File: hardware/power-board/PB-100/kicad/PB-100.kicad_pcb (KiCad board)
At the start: 4 copper layers, 150 x 90 mm, 36 parts, among them Q1 IAUT300N08S5N012ATMA2, Q101 IAUT300N08S5N012ATMA2, Q102 IAUT300N08S5N012ATMA2, Q103 IAUT300N08S5N012ATMA2, Q104 IAUT300N08S5N012ATMA2, Q105 IAUT300N08S5N012ATMA2, Q106 IAUT300N08S5N012ATMA2, Q107 IAUT300N08S5N012ATMA2, Q108 IAUT300N08S5N012ATMA2, Q109 IAUT300N08S5N012ATMA2, Q110 IAUT300N08S5N012ATMA2, Q2 IAUTN15S6N025ATMA1, U1 LM74930QRGERQ1

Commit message: feat: add dual protected fog switch inputs
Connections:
- net EXT_DIG2 renamed FOG_B_SW_IN
- net FOG_SW_IN renamed FOG_A_SW_IN
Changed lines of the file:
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@@
 	(net 15 "EXT_ADC1")
 	(net 16 "EXT_ADC2")
-	(net 17 "EXT_DIG2")
-	(net 18 "FOG_SW_IN")
+	(net 17 "FOG_A_SW_IN")
+	(net 18 "FOG_B_SW_IN")
 	(net 19 "GND")
 	(net 20 "IIN_SENSE")
@@
 			(layers "F.Cu" "F.Paste" "F.Mask")
 			(roundrect_rratio 0.200)
-			(net 18 "FOG_SW_IN")
-			(pinfunction "FOG_SW_IN")
+			(net 17 "FOG_A_SW_IN")
+			(pinfunction "FOG_A_SW_IN")
 			(pintype "passive")
 		)
@@
 			(layers "F.Cu" "F.Paste" "F.Mask")
 			(roundrect_rratio 0.200)
-			(net 17 "EXT_DIG2")
-			(pinfunction "EXT_DIG2")
-			(pintype "passive")
-		)
+			(net 18 "FOG_B_SW_IN")
+			(pinfunction "FOG_B_SW_IN")
+			(pintype "passive")
+		)

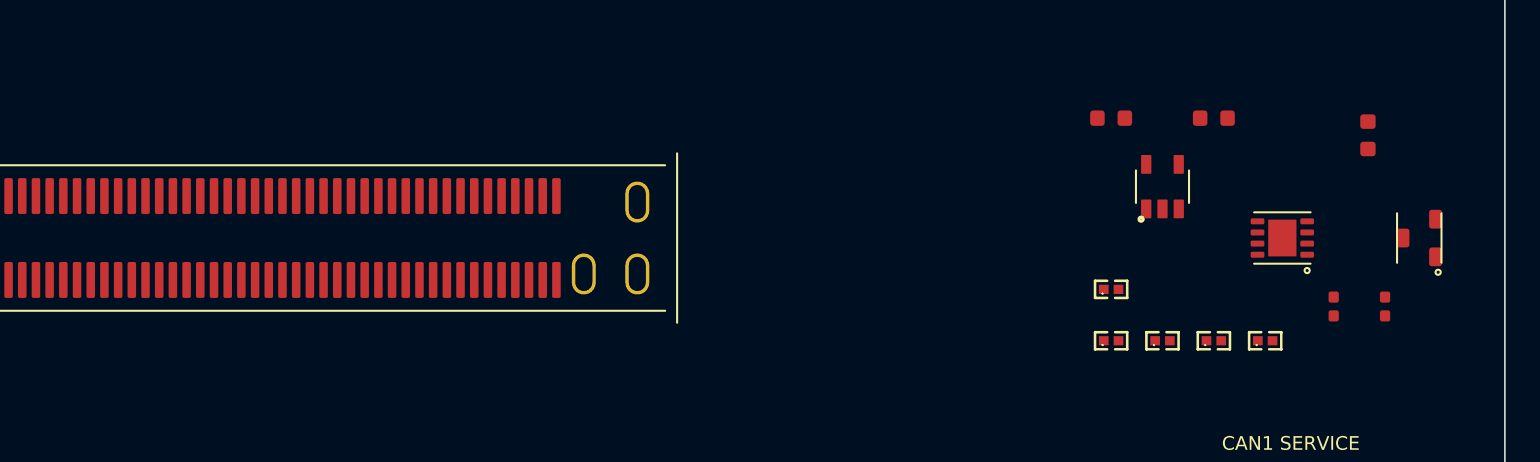
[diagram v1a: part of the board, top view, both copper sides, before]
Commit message: feat(hardware): add EVT board routing milestones
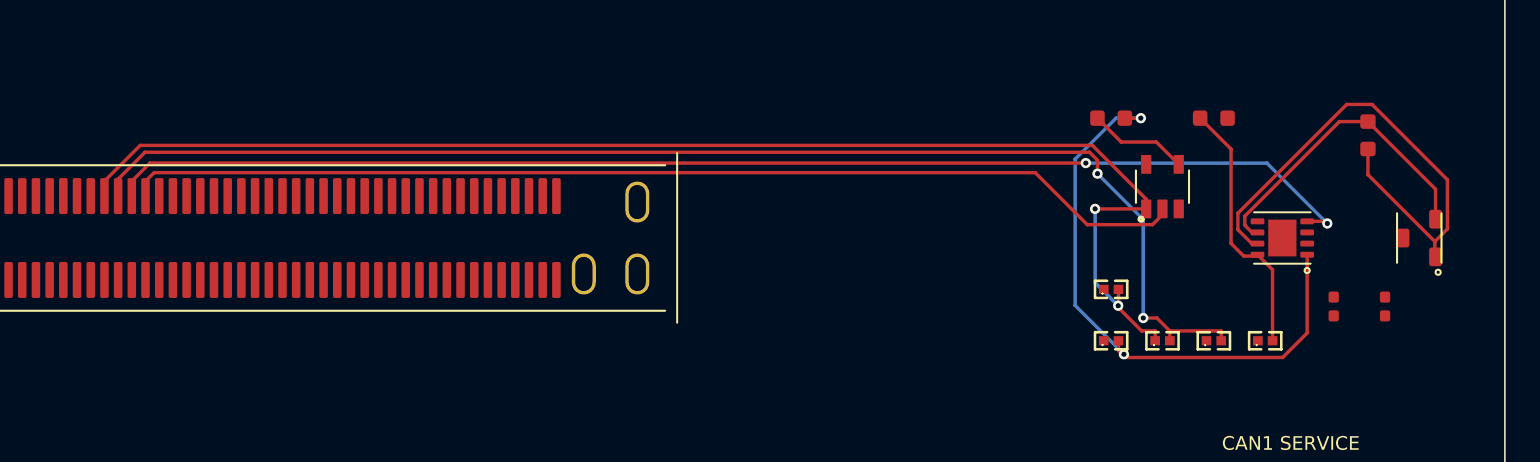
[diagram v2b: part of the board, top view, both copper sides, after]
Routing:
- net CAN1_TX_DISABLE_CMD: track 0.00 -> 78.0 mm, vias 0 -> 2
- net CAN1_TX_DISABLED_STATUS: track 0.00 -> 75.4 mm, vias 0 -> 2
- net CAN1_RX_ROUTE: track 0.00 -> 73.8 mm, vias 0 -> 2
- net CAN1_TX_ROUTE: track 0.00 -> 62.3 mm
- net CAN1_TXD_SAFE: track 0.00 -> 35.7 mm, vias 0 -> 2
- net CAN1_HARNESS_H: track 0.00 -> 31.0 mm
- net CAN1_HARNESS_L: track 0.00 -> 18.3 mm
- net CAN1_PHY_SILENT: track 0.00 -> 15.3 mm
- net CAN1_TX_GATE_OUT: track 0.00 -> 5.87 mm

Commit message: hardware: correct fog entry and EVT layout gates
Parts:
- added D_FOG1: ESD2CANFD24DBZRQ1, PB100:SOT-23-3_DBZ_TI, F.Cu at (10.0, 25.5)
- added F_FOG_12V: nanoASMDC010F 0.10A 60V DNP, PB100:PPTC_1206_3216Metric, F.Cu at (17.0, 31.0)
- added JFOG1: SEALED_DTM_3WAY_PIGTAIL_ENTRY, PB100:FOG_PIGTAIL_1x03_P3.50mm, F.Cu at (4.00, 20.0)
- added R_FOG_12V: 0R FOG 12V common DNP, PB100:R0603_DNP_LINK_1608Metric, F.Cu at (13.0, 31.0)
- added R_FOG_GND: 0R FOG dry-contact common DEFAULT, PB100:R0603_DNP_LINK_1608Metric, F.Cu at (9.00, 31.0)
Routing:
- net FOG_A_SW_IN: track 0.00 -> 82.3 mm, vias 0 -> 2
- net FOG_B_SW_IN: track 0.00 -> 81.7 mm, vias 0 -> 2
- net SW_COMMON: track 0.00 -> 25.8 mm
- net GND: track 0.00 -> 7.23 mm, vias 0 -> 2
- net CAN1_TX_DISABLE_CMD: track 78.0 -> 84.1 mm
- net CAN1_TX_DISABLED_STATUS: track 75.4 -> 80.5 mm
- net CAN1_TX_ROUTE: track 62.3 -> 67.4 mm
- net CAN1_RX_ROUTE: track 73.8 -> 78.5 mm
- net SW_12V_FUSED: track 0.00 -> 4.31 mm

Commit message: Advance PB-100 EVT routing baseline
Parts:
- added C1101: 680nF 16V X7R TMR, PB100:C0603, F.Cu at (60.7, 27.9)
- added C1102: 470nF 25V X7R BST, PB100:C0603, F.Cu at (63.9, 27.9)
- added C1103: 1nF 50V C0G ISCP, PB100:C0603, F.Cu at (67.1, 27.9)
- added C1104: 100nF 100V X7R VS, PB100:C0805, F.Cu at (48.1, 28.1)
- added C1105: 10nF 50V X7R IMON, PB100:C0603, F.Cu at (70.3, 27.9)
- added C1106: 1nF 25V DNP GATE-SLEW, PB100:C0603, F.Cu at (43.5, 30.6)
- added C1107: 1nF 100V C0G DNP SNUBBER, PB100:C0603, F.Cu at (46.6, 30.6)
- added C1201: 680nF 16V X7R TMR, PB100:C0603, F.Cu at (84.8, 27.9)
- added C1202: 470nF 25V X7R BST, PB100:C0603, F.Cu at (88.0, 27.9)
- added C1203: 1nF 50V C0G ISCP, PB100:C0603, F.Cu at (100.7, 27.9)
- added C1204: 100nF 100V X7R VS, PB100:C0805, F.Cu at (81.3, 28.1)
- added C1205: 10nF 50V X7R IMON, PB100:C0603, F.Cu at (103.9, 27.9)
- added C1206: 1nF 25V DNP GATE-SLEW, PB100:C0603, F.Cu at (78.5, 30.6)
- added C1207: 1nF 100V C0G DNP SNUBBER, PB100:C0603, F.Cu at (81.7, 30.6)
- added C1301: 680nF 16V X7R TMR, PB100:C0603, F.Cu at (19.8, 6.25)
- added C1302: 470nF 25V X7R BST, PB100:C0603, F.Cu at (22.9, 6.25)
- added C1303: 1nF 50V C0G ISCP, PB100:C0603, F.Cu at (16.1, 8.95)
- added C1304: 100nF 100V X7R VS, PB100:C0805, F.Cu at (16.4, 6.45)
- added C1305: 10nF 50V X7R IMON, PB100:C0603, F.Cu at (19.4, 8.95)
- added C1306: 1nF 25V DNP GATE-SLEW, PB100:C0603, F.Cu at (22.6, 8.95)
- added C1307: 1nF 100V C0G DNP SNUBBER, PB100:C0603, F.Cu at (13.4, 10.8)
- added C1401: 680nF 16V X7R TMR, PB100:C0603, F.Cu at (32.0, 6.25)
- added C1402: 470nF 25V X7R BST, PB100:C0603, F.Cu at (35.2, 6.25)
- added C1403: 1nF 50V C0G ISCP, PB100:C0603, F.Cu at (38.5, 6.25)
- added C1404: 100nF 100V X7R VS, PB100:C0805, F.Cu at (28.6, 6.45)
- added C1405: 10nF 50V X7R IMON, PB100:C0603, F.Cu at (32.0, 8.45)
- added C1406: 1nF 25V DNP GATE-SLEW, PB100:C0603, F.Cu at (35.2, 8.45)
- added C1407: 1nF 100V C0G DNP SNUBBER, PB100:C0603, F.Cu at (38.5, 8.45)
- added C1501: 680nF 16V X7R TMR, PB100:C0603, F.Cu at (49.9, 35.0)
- added C1502: 470nF 25V X7R BST, PB100:C0603, B.Cu at (49.0, 10.2)
- added C1503: 1nF 50V C0G ISCP, PB100:C0603, B.Cu at (52.2, 10.2)
- added C1504: 100nF 100V X7R VS, PB100:C0805, B.Cu at (45.6, 10.4)
- added C1505: 10nF 50V X7R IMON, PB100:C0603, F.Cu at (53.0, 35.0)
- added C1506: 1nF 25V DNP GATE-SLEW, PB100:C0603, F.Cu at (45.5, 36.8)
- added C1507: 1nF 100V C0G DNP SNUBBER, PB100:C0603, F.Cu at (48.6, 36.8)
- added C1601: 680nF 16V X7R TMR, PB100:C0603, F.Cu at (64.2, 6.25)
- added C1602: 470nF 25V X7R BST, PB100:C0603, B.Cu at (65.0, 2.75)
- added C1603: 1nF 50V C0G ISCP, PB100:C0603, B.Cu at (68.2, 2.75)
- added C1604: 100nF 100V X7R VS, PB100:C0805, B.Cu at (61.6, 2.95)
- added C1605: 10nF 50V X7R IMON, PB100:C0603, F.Cu at (67.3, 6.25)
- added C1606: 1nF 25V DNP GATE-SLEW, PB100:C0603, B.Cu at (71.5, 2.75)
- added C1607: 1nF 100V C0G DNP SNUBBER, PB100:C0603, B.Cu at (65.0, 4.95)
- added C1701: 680nF 16V X7R TMR, PB100:C0603, F.Cu at (77.5, 6.25)
- added C1702: 470nF 25V X7R BST, PB100:C0603, B.Cu at (83.8, 2.75)
- added C1703: 1nF 50V C0G ISCP, PB100:C0603, B.Cu at (87.0, 2.75)
- added C1704: 100nF 100V X7R VS, PB100:C0805, B.Cu at (80.3, 2.95)
- added C1705: 10nF 50V X7R IMON, PB100:C0603, F.Cu at (80.7, 6.25)
- added C1706: 1nF 25V DNP GATE-SLEW, PB100:C0603, B.Cu at (80.2, 5.45)
- added C1707: 1nF 100V C0G DNP SNUBBER, PB100:C0603, B.Cu at (83.3, 5.45)
- added C1801: 680nF 16V X7R TMR, PB100:C0603, F.Cu at (93.5, 35.0)
- added C1802: 470nF 25V X7R BST, PB100:C0603, B.Cu at (97.0, 10.2)
- added C1803: 1nF 50V C0G ISCP, PB100:C0603, B.Cu at (100.2, 10.2)
- added C1804: 100nF 100V X7R VS, PB100:C0805, B.Cu at (93.7, 10.4)
- added C1805: 10nF 50V X7R IMON, PB100:C0603, F.Cu at (93.5, 36.8)
- added C1806: 1nF 25V DNP GATE-SLEW, PB100:C0603, B.Cu at (103.5, 10.2)
- added C1807: 1nF 100V C0G DNP SNUBBER, PB100:C0603, F.Cu at (103.8, 36.8)
- added C1901: 680nF 16V X7R TMR, PB100:C0603, F.Cu at (113.0, 33.0)
- added C1902: 470nF 25V X7R BST, PB100:C0603, F.Cu at (109.5, 35.2)
- added C1903: 1nF 50V C0G ISCP, PB100:C0603, F.Cu at (112.7, 35.2)
- added C1904: 100nF 100V X7R VS, PB100:C0805, F.Cu at (109.7, 33.2)
- added C1905: 10nF 50V X7R IMON, PB100:C0603, F.Cu at (109.5, 37.0)
- added C1906: 1nF 25V DNP GATE-SLEW, PB100:C0603, F.Cu at (112.7, 37.0)
- added C1907: 1nF 100V C0G DNP SNUBBER, PB100:C0603, F.Cu at (115.8, 37.0)
- added C20: 100nF 50V X7R DIFF, PB100:C0603, B.Cu at (26.3, 25.1)
- added C2001: 680nF 16V X7R TMR, PB100:C0603, F.Cu at (132.8, 6.25)
- added C2002: 470nF 25V X7R BST, PB100:C0603, F.Cu at (135.9, 6.25)
- added C2003: 1nF 50V C0G ISCP, PB100:C0603, F.Cu at (129.2, 8.95)
- added C2004: 100nF 100V X7R VS, PB100:C0805, F.Cu at (129.3, 6.45)
- added C2005: 10nF 50V X7R IMON, PB100:C0603, F.Cu at (132.3, 8.95)
- added C2006: 1nF 25V DNP GATE-SLEW, PB100:C0603, F.Cu at (135.6, 8.95)
- added C2007: 1nF 100V C0G DNP SNUBBER, PB100:C0603, F.Cu at (129.4, 10.8)
- added C21: 1nF 100V C0G, PB100:C0603, B.Cu at (29.5, 25.1)
- added C22: 100nF 16V X7R, PB100:C0603, B.Cu at (32.7, 25.1)
- added C23: 1nF PB I2C INT FILTER DNP, PB100:C0603, B.Cu at (7.55, 27.9)
- added C24: 10nF 50V X7R, PB100:C0603, B.Cu at (10.8, 27.9)
- added C30: 2.2uF 100V X7R, PB100:C1210, F.Cu at (114.0, 8.00)
- added C31: 100nF 100V X7R, PB100:C0805, F.Cu at (118.0, 8.00)
- added C32: 10uF 100V BULK CANDIDATE, PB100:C1210, F.Cu at (114.0, 15.5)
- added C33: 2.2nF 50V X7R, PB100:C0603, F.Cu at (119.0, 14.0)
- added C34: 22uF 10V X7R, PB100:C1210, F.Cu at (137.0, 22.0)
- added C35: 22uF 10V X7R, PB100:C1210, F.Cu at (137.0, 28.0)
- added C36: 100nF 16V X7R, PB100:C0603, F.Cu at (137.0, 34.0)
- added C37: 10nF PGOOD FILTER DNP, PB100:C0603, B.Cu at (121.5, 43.5)
- added C38: 3.3nF 100V C0G TYPE3 CA, PB100:C0603, F.Cu at (144.0, 15.0)
- added C39: 180pF 50V C0G TYPE3 CB, PB100:C0603, F.Cu at (144.0, 23.0)
- added C40: 1nF 100V C0G DNP, PB100:C0603, F.Cu at (132.0, 34.0)
- added C61: 10nF 50V X7R, PB100:C0603, B.Cu at (124.7, 43.5)
- added C64: 10nF 50V X7R, PB100:C0603, B.Cu at (127.8, 43.5)
- added C67: 10nF 50V X7R, PB100:C0603, B.Cu at (131.1, 43.5)
- added CCAP1: 100nF 25V X7R, PB100:C0603, B.Cu at (13.9, 27.9)
- added CSN1: 1nF 100V C0G DNP, PB100:C0603, B.Cu at (17.1, 27.9)
- added CSN2: 1nF 200V C0G DNP, PB100:C0603, B.Cu at (20.4, 27.9)
- added CVS1: CGA6N3X7R2A225M230AE 2.2uF 100V X7R; Ceff>=1uF@56V, PB100:C1210, B.Cu at (8.57, 22.6)
- added DCL101: STPS40170CGY-TR 2x20A 170V COMMON-CATHODE, PB100:D2PAK_3_CommonCathode, F.Cu at (68.0, 16.0)
- added DCL102: STPS40170CGY-TR 2x20A 170V COMMON-CATHODE, PB100:D2PAK_3_CommonCathode, F.Cu at (82.0, 16.0)
- added DCL103: STPS40170CGY-TR 2x20A 170V COMMON-CATHODE, PB100:D2PAK_3_CommonCathode, B.Cu at (16.0, 75.0)
- added DCL104: STPS40170CGY-TR 2x20A 170V COMMON-CATHODE, PB100:D2PAK_3_CommonCathode, B.Cu at (30.0, 75.0)
- added DCL105: STPS40170CGY-TR 2x20A 170V COMMON-CATHODE, PB100:D2PAK_3_CommonCathode, B.Cu at (51.0, 75.0)
- added DCL106: STPS40170CGY-TR 2x20A 170V COMMON-CATHODE, PB100:D2PAK_3_CommonCathode, B.Cu at (67.0, 75.0)
- added DCL107: STPS40170CGY-TR 2x20A 170V COMMON-CATHODE, PB100:D2PAK_3_CommonCathode, B.Cu at (83.0, 75.0)
- added DCL108: STPS40170CGY-TR 2x20A 170V COMMON-CATHODE, PB100:D2PAK_3_CommonCathode, B.Cu at (99.0, 75.0)
- added DCL109: STPS40170CGY-TR 2x20A 170V COMMON-CATHODE, PB100:D2PAK_3_CommonCathode, B.Cu at (120.0, 75.0)
- added DCL110: STPS40170CGY-TR 2x20A 170V COMMON-CATHODE, PB100:D2PAK_3_CommonCathode, B.Cu at (134.0, 75.0)
- added DZVS1: 56V AUTOMOTIVE ZENER, PB100:SOD-123F, B.Cu at (14.0, 22.4)
- added JIN1: 40A PCB PIGTAIL TO NEAR-BATTERY 50A FUSE, PB100:POWER_PIGTAIL_2xTH_40A, F.Cu at (6.50, 45.0)
- added JISO1: EVT INPUT-STAGE ISOLATION LINK — FITTED FOR NORMAL EVT, PB100:EVT_INPUT_ISOLATION_LINK_M4, F.Cu at (34.0, 44.0)
- added L1: 47uH SHIELDED AEC-Q200; Isat>=2.2A Irms>=1.2A, PB100:Inductor_12x12mm, F.Cu at (126.0, 25.0)
- added QT101: MMBT3904-Q REMOTE TEMP DIODE, PB100:SOT-23-3_DBZ_TI, F.Cu at (46.3, 22.6)
- added QT102: MMBT3904-Q REMOTE TEMP DIODE, PB100:SOT-23-3_DBZ_TI, F.Cu at (103.0, 22.6)
- added QT103: MMBT3904-Q REMOTE TEMP DIODE, PB100:SOT-23-3_DBZ_TI, F.Cu at (14.5, 3.60)
- added QT104: MMBT3904-Q REMOTE TEMP DIODE, PB100:SOT-23-3_DBZ_TI, F.Cu at (29.5, 3.60)
- added QT105: MMBT3904-Q REMOTE TEMP DIODE, PB100:SOT-23-3_DBZ_TI, F.Cu at (46.5, 11.1)
- added QT106: MMBT3904-Q REMOTE TEMP DIODE, PB100:SOT-23-3_DBZ_TI, F.Cu at (62.5, 3.60)
- added QT107: MMBT3904-Q REMOTE TEMP DIODE, PB100:SOT-23-3_DBZ_TI, F.Cu at (78.5, 3.60)
- added QT108: MMBT3904-Q REMOTE TEMP DIODE, PB100:SOT-23-3_DBZ_TI, F.Cu at (103.0, 11.1)
- added QT109: MMBT3904-Q REMOTE TEMP DIODE, PB100:SOT-23-3_DBZ_TI, F.Cu at (110.5, 30.4)
- added QT110: MMBT3904-Q REMOTE TEMP DIODE, PB100:SOT-23-3_DBZ_TI, F.Cu at (127.5, 3.60)
- added R1101: 470k 1%, PB100:R0603, F.Cu at (64.2, 30.6)
- added R1102: 103k 1%, PB100:R0603, F.Cu at (67.3, 30.6)
- added R1103: 12.4k 1%, PB100:R0603, F.Cu at (70.5, 30.6)
- added R1104: 100R 1% RSET, PB100:R0603, F.Cu at (43.5, 32.5)
- added R1105: 49.9k 1% RIWRN, PB100:R0603, F.Cu at (46.6, 32.5)
- added R1106: 3.40k 1% RISCP, PB100:R0603, F.Cu at (64.2, 32.5)
- added R1107: 12.1k 1% RIMON, PB100:R0603, F.Cu at (67.3, 32.5)
- added R1108: 1k 1% IMON ADC SERIES, PB100:R0603, F.Cu at (70.5, 32.5)
- added R1109: 100k CTL DEFAULT-OFF, PB100:R0603, F.Cu at (43.5, 34.2)
- added R1110: 3.3R 1% REPLACEABLE PU, PB100:R0603, F.Cu at (46.6, 34.2)
- added R1111: 0R REPLACEABLE PD, PB100:R0603, F.Cu at (64.2, 34.2)
- added R1112: 10k FLT PULL-UP, PB100:R0603, F.Cu at (67.3, 34.2)
- added R1113: 100R DNP DRAIN-SOURCE SNUBBER, PB100:R0603, F.Cu at (70.5, 34.2)
- added R1201: 470k 1%, PB100:R0603, F.Cu at (84.8, 30.6)
- added R1202: 103k 1%, PB100:R0603, F.Cu at (88.0, 30.6)
- added R1203: 12.4k 1%, PB100:R0603, F.Cu at (104.2, 30.6)
- added R1204: 100R 1% RSET, PB100:R0603, F.Cu at (78.5, 32.5)
- added R1205: 67.3k 1% RIWRN, PB100:R0603, F.Cu at (81.7, 32.5)
- added R1206: 2.61k 1% RISCP, PB100:R0603, F.Cu at (84.8, 32.5)
- added R1207: 12.1k 1% RIMON, PB100:R0603, F.Cu at (88.0, 32.5)
- added R1208: 1k 1% IMON ADC SERIES, PB100:R0603, F.Cu at (104.2, 32.5)
- added R1209: 100k CTL DEFAULT-OFF, PB100:R0603, F.Cu at (78.5, 34.2)
- added R1210: 3.3R 1% REPLACEABLE PU, PB100:R0603, F.Cu at (81.7, 34.2)
- added R1211: 0R REPLACEABLE PD, PB100:R0603, F.Cu at (84.8, 34.2)
- added R1212: 10k FLT PULL-UP, PB100:R0603, F.Cu at (88.0, 34.2)
- added R1213: 100R DNP DRAIN-SOURCE SNUBBER, PB100:R0603, F.Cu at (104.2, 34.2)
- added R1301: 470k 1%, PB100:R0603, F.Cu at (16.6, 10.8)
- added R1302: 103k 1%, PB100:R0603, F.Cu at (19.9, 10.8)
- added R1303: 12.4k 1%, PB100:R0603, F.Cu at (23.1, 10.8)
- added R1304: 100R 1% RSET, PB100:R0603, F.Cu at (13.4, 12.6)
- added R1305: 49.9k 1% RIWRN, PB100:R0603, F.Cu at (16.6, 12.6)
- added R1306: 3.83k 1% RISCP, PB100:R0603, F.Cu at (19.9, 12.6)
- added R1307: 12.1k 1% RIMON, PB100:R0603, F.Cu at (23.1, 12.6)
- added R1308: 1k 1% IMON ADC SERIES, PB100:R0603, F.Cu at (13.4, 14.3)
- added R1309: 100k CTL DEFAULT-OFF, PB100:R0603, F.Cu at (16.6, 14.3)
- added R1310: 3.3R 1% REPLACEABLE PU, PB100:R0603, F.Cu at (19.9, 14.3)
- added R1311: 0R REPLACEABLE PD, PB100:R0603, F.Cu at (23.1, 14.3)
- added R1312: 10k FLT PULL-UP, PB100:R0603, F.Cu at (13.4, 16.1)
- added R1313: 100R DNP DRAIN-SOURCE SNUBBER, PB100:R0603, F.Cu at (16.6, 16.1)
- added R1401: 470k 1%, PB100:R0603, F.Cu at (28.4, 10.2)
- added R1402: 103k 1%, PB100:R0603, F.Cu at (31.6, 10.2)
- added R1403: 12.4k 1%, PB100:R0603, F.Cu at (34.9, 10.2)
- added R1404: 100R 1% RSET, PB100:R0603, F.Cu at (38.0, 10.2)
- added R1405: 49.9k 1% RIWRN, PB100:R0603, F.Cu at (41.2, 10.2)
- added R1406: 3.83k 1% RISCP, PB100:R0603, F.Cu at (28.4, 12.1)
- added R1407: 12.1k 1% RIMON, PB100:R0603, F.Cu at (31.6, 12.1)
- added R1408: 1k 1% IMON ADC SERIES, PB100:R0603, F.Cu at (34.9, 12.1)
- added R1409: 100k CTL DEFAULT-OFF, PB100:R0603, F.Cu at (38.0, 12.1)
- added R1410: 3.3R 1% REPLACEABLE PU, PB100:R0603, F.Cu at (41.2, 12.1)
- added R1411: 0R REPLACEABLE PD, PB100:R0603, F.Cu at (28.4, 13.8)
- added R1412: 10k FLT PULL-UP, PB100:R0603, F.Cu at (31.6, 13.8)
- added R1413: 100R DNP DRAIN-SOURCE SNUBBER, PB100:R0603, F.Cu at (34.9, 13.8)
- added R1501: 470k 1%, PB100:R0603, F.Cu at (51.9, 36.8)
- added R1502: 103k 1%, PB100:R0603, F.Cu at (55.0, 36.8)
- added R1503: 12.4k 1%, PB100:R0603, F.Cu at (45.5, 38.8)
- added R1504: 100R 1% RSET, PB100:R0603, F.Cu at (45.5, 40.5)
- added R1505: 49.9k 1% RIWRN, PB100:R0603, F.Cu at (45.5, 42.4)
- added R1506: 3.74k 1% RISCP, PB100:R0603, F.Cu at (45.5, 44.1)
- added R1507: 12.1k 1% RIMON, PB100:R0603, F.Cu at (45.5, 46.0)
- added R1508: 1k 1% IMON ADC SERIES, PB100:R0603, F.Cu at (45.5, 47.8)
- added R1509: 100k CTL DEFAULT-OFF, PB100:R0603, F.Cu at (47.8, 51.8)
- added R1510: 3.3R 1% REPLACEABLE PU, PB100:R0603, F.Cu at (51.0, 51.8)
- added R1511: 0R REPLACEABLE PD, PB100:R0603, F.Cu at (54.1, 51.8)
- added R1512: 10k FLT PULL-UP, PB100:R0603, F.Cu at (50.4, 53.5)
- added R1513: 100R DNP DRAIN-SOURCE SNUBBER, PB100:R0603, F.Cu at (53.5, 53.5)
- added R1601: 470k 1%, PB100:R0603, F.Cu at (70.5, 6.25)
- added R1602: 103k 1%, PB100:R0603, F.Cu at (63.8, 36.1)
- added R1603: 12.4k 1%, PB100:R0603, F.Cu at (67.0, 36.1)
- added R1604: 100R 1% RSET, PB100:R0603, B.Cu at (68.2, 4.95)
- added R1605: 49.9k 1% RIWRN, PB100:R0603, F.Cu at (70.2, 36.1)
- added R1606: 3.83k 1% RISCP, PB100:R0603, B.Cu at (71.5, 4.95)
- added R1607: 12.1k 1% RIMON, PB100:R0603, F.Cu at (61.5, 51.8)
- added R1608: 1k 1% IMON ADC SERIES, PB100:R0603, F.Cu at (64.7, 51.8)
- added R1609: 100k CTL DEFAULT-OFF, PB100:R0603, F.Cu at (67.8, 51.8)
- added R1610: 3.3R 1% REPLACEABLE PU, PB100:R0603, B.Cu at (61.5, 6.75)
- added R1611: 0R REPLACEABLE PD, PB100:R0603, B.Cu at (64.7, 6.75)
- added R1612: 10k FLT PULL-UP, PB100:R0603, F.Cu at (71.0, 51.8)
- added R1613: 100R DNP DRAIN-SOURCE SNUBBER, PB100:R0603, B.Cu at (67.8, 6.75)
- added R1701: 470k 1%, PB100:R0603, F.Cu at (83.8, 6.25)
- added R1702: 103k 1%, PB100:R0603, F.Cu at (87.0, 6.25)
- added R1703: 12.4k 1%, PB100:R0603, F.Cu at (77.5, 8.05)
- added R1704: 100R 1% RSET, PB100:R0603, B.Cu at (86.5, 5.45)
- added R1705: 49.9k 1% RIWRN, PB100:R0603, F.Cu at (80.7, 8.05)
- added R1706: 3.83k 1% RISCP, PB100:R0603, B.Cu at (77.5, 7.25)
- added R1707: 12.1k 1% RIMON, PB100:R0603, F.Cu at (83.8, 8.05)
- added R1708: 1k 1% IMON ADC SERIES, PB100:R0603, F.Cu at (87.0, 8.05)
- added R1709: 100k CTL DEFAULT-OFF, PB100:R0603, F.Cu at (77.5, 36.1)
- added R1710: 3.3R 1% REPLACEABLE PU, PB100:R0603, B.Cu at (80.7, 7.25)
- added R1711: 0R REPLACEABLE PD, PB100:R0603, B.Cu at (83.8, 7.25)
- added R1712: 10k FLT PULL-UP, PB100:R0603, F.Cu at (80.7, 36.1)
- added R1713: 100R DNP DRAIN-SOURCE SNUBBER, PB100:R0603, B.Cu at (87.0, 7.25)
- added R1801: 470k 1%, PB100:R0603, F.Cu at (103.8, 38.8)
- added R1802: 103k 1%, PB100:R0603, F.Cu at (103.8, 40.5)
- added R1803: 12.4k 1%, PB100:R0603, F.Cu at (103.8, 42.4)
- added R1804: 100R 1% RSET, PB100:R0603, F.Cu at (103.8, 44.1)
- added R1805: 49.9k 1% RIWRN, PB100:R0603, F.Cu at (103.8, 46.0)
- added R1806: 3.74k 1% RISCP, PB100:R0603, F.Cu at (103.8, 47.8)
- added R1807: 12.1k 1% RIMON, PB100:R0603, F.Cu at (103.8, 49.5)
- added R1808: 1k 1% IMON ADC SERIES, PB100:R0603, F.Cu at (93.5, 51.8)
- added R1809: 100k CTL DEFAULT-OFF, PB100:R0603, F.Cu at (96.7, 51.8)
- added R1810: 3.3R 1% REPLACEABLE PU, PB100:R0603, F.Cu at (99.8, 51.8)
- added R1811: 0R REPLACEABLE PD, PB100:R0603, F.Cu at (103.0, 51.8)
- added R1812: 10k FLT PULL-UP, PB100:R0603, F.Cu at (98.3, 53.5)
- added R1813: 100R DNP DRAIN-SOURCE SNUBBER, PB100:R0603, F.Cu at (101.5, 53.5)
- added R1901: 470k 1%, PB100:R0603, F.Cu at (119.0, 37.0)
- added R1902: 103k 1%, PB100:R0603, F.Cu at (109.5, 39.0)
- added R1903: 12.4k 1%, PB100:R0603, F.Cu at (112.7, 39.0)
- added R1904: 100R 1% RSET, PB100:R0603, F.Cu at (115.8, 39.0)
- added R1905: 49.9k 1% RIWRN, PB100:R0603, F.Cu at (119.0, 39.0)
- added R1906: 3.74k 1% RISCP, PB100:R0603, F.Cu at (109.5, 40.9)
- added R1907: 12.1k 1% RIMON, PB100:R0603, F.Cu at (112.7, 40.9)
- added R1908: 1k 1% IMON ADC SERIES, PB100:R0603, F.Cu at (115.8, 40.9)
- added R1909: 100k CTL DEFAULT-OFF, PB100:R0603, F.Cu at (119.0, 40.9)
- added R1910: 3.3R 1% REPLACEABLE PU, PB100:R0603, F.Cu at (109.5, 42.6)
- added R1911: 0R REPLACEABLE PD, PB100:R0603, F.Cu at (112.7, 42.6)
- added R1912: 10k FLT PULL-UP, PB100:R0603, F.Cu at (115.8, 42.6)
- added R1913: 100R DNP DRAIN-SOURCE SNUBBER, PB100:R0603, F.Cu at (119.0, 42.6)
- added R20: 10R 0.1% SHUNT FILTER, PB100:R0603, B.Cu at (23.6, 27.9)
- added R2001: 470k 1%, PB100:R0603, F.Cu at (132.6, 10.8)
- added R2002: 103k 1%, PB100:R0603, F.Cu at (135.8, 10.8)
- added R2003: 12.4k 1%, PB100:R0603, F.Cu at (129.4, 12.6)
- added R2004: 100R 1% RSET, PB100:R0603, F.Cu at (132.6, 12.6)
- added R2005: 49.9k 1% RIWRN, PB100:R0603, F.Cu at (135.8, 12.6)
- added R2006: 3.83k 1% RISCP, PB100:R0603, F.Cu at (129.4, 14.3)
- added R2007: 12.1k 1% RIMON, PB100:R0603, F.Cu at (132.6, 14.3)
- added R2008: 1k 1% IMON ADC SERIES, PB100:R0603, F.Cu at (135.8, 14.3)
- added R2009: 100k CTL DEFAULT-OFF, PB100:R0603, F.Cu at (129.4, 16.1)
- added R2010: 3.3R 1% REPLACEABLE PU, PB100:R0603, F.Cu at (132.6, 16.1)
- added R2011: 0R REPLACEABLE PD, PB100:R0603, F.Cu at (135.8, 16.1)
- added R2012: 10k FLT PULL-UP, PB100:R0603, F.Cu at (134.9, 17.9)
- added R2013: 100R DNP DRAIN-SOURCE SNUBBER, PB100:R0603, F.Cu at (138.1, 17.9)
- added R21: 10R 0.1% SHUNT FILTER, PB100:R0603, B.Cu at (26.8, 27.9)
- added R22: 1k 1% VBUS FILTER, PB100:R0603, B.Cu at (29.9, 27.9)
- added R23: 10k PB I2C SDA PULL DNP, PB100:R0603, B.Cu at (33.1, 27.9)
- added R24: 10k PB I2C SCL PULL DNP, PB100:R0603, B.Cu at (7.55, 29.6)
- added R25: 47k PB I2C INT PULL DNP, PB100:R0603, B.Cu at (10.8, 29.6)
- added R26: 0R INPUT FAULT AGGREGATE, PB100:R0603, B.Cu at (13.9, 29.6)
- added R27: 200k 0.1% 100V, PB100:R0603, B.Cu at (17.1, 29.6)
- added R28: 10k 0.1%, PB100:R0603, B.Cu at (20.4, 29.6)
- added R29: 1k 0.1%, PB100:R0603, B.Cu at (23.6, 29.6)
- added R3: 42.2k 1%, PB100:R0603, B.Cu at (26.8, 29.6)
- added R30: 332k 1%, PB100:R0603, F.Cu at (114.0, 3.00)
- added R31: 100k 1%, PB100:R0603, F.Cu at (118.0, 3.00)
- added R32: 41.2k 1%, PB100:R0603, F.Cu at (122.0, 3.00)
- added R33: 158k 0.1%, PB100:R0603, F.Cu at (118.0, 34.0)
- added R34: 49.9k 0.1%, PB100:R0603, F.Cu at (122.0, 34.0)
- added R35: 47k PGOOD PULL-UP, PB100:R0603, B.Cu at (134.2, 43.5)
- added R36: 110k 1% TYPE3 RA, PB100:R0603, F.Cu at (144.0, 19.0)
- added R37: 100R BUCK SNUBBER DNP, PB100:R0603, F.Cu at (128.0, 34.0)
- added R4: 42.2k 1%, PB100:R0603, B.Cu at (29.9, 29.6)
- added R5: 1.00k 1%, PB100:R0603, B.Cu at (33.1, 29.6)
- added R6: 10k 1%, PB100:R0603, B.Cu at (3.45, 31.4)
- added R61: 4.7k 1% AEC-Q200, PB100:R0603, B.Cu at (137.4, 43.5)
- added R62: 1k 1% ADC SERIES, PB100:R0603, B.Cu at (140.7, 43.5)
- added R64: 4.7k 1% AEC-Q200, PB100:R0603, B.Cu at (143.8, 43.5)
- added R65: 1k 1% ADC SERIES, PB100:R0603, B.Cu at (121.5, 45.2)
- added R67: 4.7k 1% AEC-Q200, PB100:R0603, B.Cu at (124.7, 45.2)
- added R68: 1k 1% ADC SERIES, PB100:R0603, B.Cu at (127.8, 45.2)
- added R7: 0R REPLACEABLE Q1 GATE, PB100:R0603, B.Cu at (6.65, 31.4)
- added R8: 0R REPLACEABLE Q2 GATE, PB100:R0603, B.Cu at (9.85, 31.4)
- added RID1: PB REV1 ID: 10k/10k 0.1% DIVIDER, PB100:Board_ID_Divider_0603x2, B.Cu at (123.2, 38.4)
- added RSH1: CSS4J-4026R-L500F 0.5mR 5W FOUR-TERMINAL, PB100:CSS4J-4026_Bourns, B.Cu at (27.0, 60.0)
- added RSH101: CSS4J-4026 1.0mR FOUR-TERMINAL, PB100:CSS4J-4026_Bourns, F.Cu at (55.0, 28.0)
- added RSH102: CSS4J-4026 0.5mR FOUR-TERMINAL, PB100:CSS4J-4026_Bourns, F.Cu at (95.0, 28.0)
- added RSH103: CSS4J-4026 1.5mR FOUR-TERMINAL, PB100:CSS4J-4026_Bourns, F.Cu at (19.0, 64.0)
- added RSH104: CSS4J-4026 1.5mR FOUR-TERMINAL, PB100:CSS4J-4026_Bourns, F.Cu at (32.4, 62.0)
- added RSH105: CSS4J-4026 3.0mR FOUR-TERMINAL, PB100:CSS4J-4026_Bourns, F.Cu at (51.0, 62.0)
- added RSH106: CSS4J-4026 1.5mR FOUR-TERMINAL, PB100:CSS4J-4026_Bourns, F.Cu at (67.0, 62.0)
- added RSH107: CSS4J-4026 1.5mR FOUR-TERMINAL, PB100:CSS4J-4026_Bourns, F.Cu at (83.0, 62.0)
- added RSH108: CSS4J-4026 3.0mR FOUR-TERMINAL, PB100:CSS4J-4026_Bourns, F.Cu at (99.0, 62.0)
- added RSH109: CSS4J-4026 3.0mR FOUR-TERMINAL, PB100:CSS4J-4026_Bourns, F.Cu at (120.0, 62.0)
- added RSH110: CSS4J-4026 1.5mR FOUR-TERMINAL, PB100:CSS4J-4026_Bourns, F.Cu at (131.0, 62.0)
- added RSN1: 100R DNP Q1 DAMPING, PB100:R0603, B.Cu at (13.1, 31.4)
- added RSN2: 100R DNP Q2 DAMPING, PB100:R0603, B.Cu at (16.2, 31.4)
- added RT1: NTCGS103JF103FT8 10k 1% B3435 AEC-Q200, PB100:R0402, B.Cu at (130.3, 44.8)
- added RT2: NTCGS103JF103FT8 10k 1% B3435 AEC-Q200, PB100:R0402, B.Cu at (132.0, 44.8)
- added RT3: NTCGS103JF103FT8 10k 1% B3435 AEC-Q200, PB100:R0402, B.Cu at (133.8, 44.8)
- added TP001: TEST GND, PB100:TestPoint_SMD_1.5mm, B.Cu at (18.1, 22.2)
- added TP002: TEST AGND, PB100:TestPoint_SMD_1.5mm, B.Cu at (127.9, 38.2)
- added TP003: TEST VBAT_RAW, PB100:TestPoint_SMD_1.5mm, B.Cu at (20.9, 22.2)
- added TP004: TEST VBAT_REV_PROT, PB100:TestPoint_SMD_1.5mm, B.Cu at (23.6, 22.2)
- added TP005: TEST VBAT_PROT, PB100:TestPoint_SMD_1.5mm, B.Cu at (26.2, 22.2)
- added TP006: TEST IIN_SHUNT_HI, PB100:TestPoint_SMD_1.5mm, B.Cu at (28.9, 22.2)
- added TP007: TEST IIN_SHUNT_LO, PB100:TestPoint_SMD_1.5mm, B.Cu at (31.6, 22.2)
- added TP008: TEST VBAT_SENSE, PB100:TestPoint_SMD_1.5mm, B.Cu at (34.4, 22.2)
- added TP009: TEST IIN_SENSE, PB100:TestPoint_SMD_1.5mm, B.Cu at (12.6, 25.6)
- added TP010: TEST PB_5V_OUT, PB100:TestPoint_SMD_1.5mm, B.Cu at (130.6, 38.2)
- added TP011: TEST PB_PWR_GOOD, PB100:TestPoint_SMD_1.5mm, B.Cu at (133.3, 38.2)
- added TP012: TEST LB_3V3_IO, PB100:TestPoint_SMD_1.5mm, B.Cu at (121.2, 41.2)
- added TP013: TEST PB_I2C_SCL, PB100:TestPoint_SMD_1.5mm, B.Cu at (123.9, 41.2)
- added TP014: TEST PB_I2C_SDA, PB100:TestPoint_SMD_1.5mm, B.Cu at (126.6, 41.2)
- added TP015: TEST PB_I2C_INT, PB100:TestPoint_SMD_1.5mm, B.Cu at (129.3, 41.2)
- added TP016: TEST TEMP_PCB, PB100:TestPoint_SMD_1.5mm, B.Cu at (132.0, 41.2)
- added TP017: TEST TEMP_PWR_A, PB100:TestPoint_SMD_1.5mm, B.Cu at (134.7, 41.2)
- added TP018: TEST TEMP_PWR_B, PB100:TestPoint_SMD_1.5mm, B.Cu at (137.4, 41.2)
- added TP019: TEST CAN1_TX_DISABLE_CMD, PB100:TestPoint_SMD_1.5mm, B.Cu at (140.1, 41.2)
- added TP020: TEST CAN1_TX_DISABLED_STATUS, PB100:TestPoint_SMD_1.5mm, B.Cu at (142.8, 41.2)
- added TP021: TEST CAN1_RX_ROUTE, PB100:TestPoint_SMD_1.5mm, B.Cu at (145.5, 41.2)
- added TP022: TEST OUT1_CTL, PB100:TestPoint_SMD_1.5mm, F.Cu at (45.0, 25.7)
- added TP023: TEST OUT1_FLT, PB100:TestPoint_SMD_1.5mm, F.Cu at (47.7, 25.7)
- added TP024: TEST OUT1_IMON, PB100:TestPoint_SMD_1.5mm, F.Cu at (60.5, 25.7)
- added TP025: TEST OUT1_SWITCHED, PB100:TestPoint_SMD_1.5mm, F.Cu at (45.0, 28.4)
- added TP026: TEST OUT2_CTL, PB100:TestPoint_SMD_1.5mm, F.Cu at (89.2, 25.7)
- added TP027: TEST OUT2_FLT, PB100:TestPoint_SMD_1.5mm, F.Cu at (100.5, 25.7)
- added TP028: TEST OUT2_IMON, PB100:TestPoint_SMD_1.5mm, F.Cu at (103.2, 25.7)
- added TP029: TEST OUT2_SWITCHED, PB100:TestPoint_SMD_1.5mm, F.Cu at (78.2, 28.4)
- added TP030: TEST OUT3_CTL, PB100:TestPoint_SMD_1.5mm, F.Cu at (18.5, 3.20)
- added TP031: TEST OUT3_FLT, PB100:TestPoint_SMD_1.5mm, F.Cu at (21.2, 3.20)
- added TP032: TEST OUT3_IMON, PB100:TestPoint_SMD_1.5mm, F.Cu at (23.9, 3.20)
- added TP033: TEST OUT3_SWITCHED, PB100:TestPoint_SMD_1.5mm, F.Cu at (13.2, 6.70)
- added TP034: TEST OUT4_CTL, PB100:TestPoint_SMD_1.5mm, F.Cu at (33.5, 3.20)
- added TP035: TEST OUT4_FLT, PB100:TestPoint_SMD_1.5mm, F.Cu at (36.2, 3.20)
- added TP036: TEST OUT4_IMON, PB100:TestPoint_SMD_1.5mm, F.Cu at (38.9, 3.20)
- added TP037: TEST OUT4_SWITCHED, PB100:TestPoint_SMD_1.5mm, F.Cu at (41.6, 3.20)
- added TP038: TEST OUT5_CTL, PB100:TestPoint_SMD_1.5mm, F.Cu at (45.2, 14.2)
- added TP039: TEST OUT5_FLT, PB100:TestPoint_SMD_1.5mm, F.Cu at (47.9, 14.2)
- added TP040: TEST OUT5_IMON, PB100:TestPoint_SMD_1.5mm, F.Cu at (45.2, 17.2)
- added TP041: TEST OUT5_SWITCHED, PB100:TestPoint_SMD_1.5mm, F.Cu at (47.9, 17.2)
- added TP042: TEST OUT6_CTL, PB100:TestPoint_SMD_1.5mm, F.Cu at (66.5, 3.20)
- added TP043: TEST OUT6_FLT, PB100:TestPoint_SMD_1.5mm, F.Cu at (69.2, 3.20)
- added TP044: TEST OUT6_IMON, PB100:TestPoint_SMD_1.5mm, F.Cu at (71.9, 3.20)
- added TP045: TEST OUT6_SWITCHED, PB100:TestPoint_SMD_1.5mm, F.Cu at (61.2, 6.70)
- added TP046: TEST OUT7_CTL, PB100:TestPoint_SMD_1.5mm, B.Cu at (77.2, 3.20)
- added TP047: TEST OUT7_FLT, PB100:TestPoint_SMD_1.5mm, F.Cu at (82.5, 3.20)
- added TP048: TEST OUT7_IMON, PB100:TestPoint_SMD_1.5mm, F.Cu at (85.2, 3.20)
- added TP049: TEST OUT7_SWITCHED, PB100:TestPoint_SMD_1.5mm, F.Cu at (87.9, 3.20)
- added TP050: TEST OUT8_CTL, PB100:TestPoint_SMD_1.5mm, F.Cu at (101.7, 14.2)
- added TP051: TEST OUT8_FLT, PB100:TestPoint_SMD_1.5mm, F.Cu at (104.4, 14.2)
- added TP052: TEST OUT8_IMON, PB100:TestPoint_SMD_1.5mm, F.Cu at (101.7, 17.2)
- added TP053: TEST OUT8_SWITCHED, PB100:TestPoint_SMD_1.5mm, F.Cu at (104.4, 17.2)
- added TP054: TEST OUT9_CTL, PB100:TestPoint_SMD_1.5mm, F.Cu at (109.2, 18.2)
- added TP055: TEST OUT9_FLT, PB100:TestPoint_SMD_1.5mm, F.Cu at (117.0, 18.2)
- added TP056: TEST OUT9_IMON, PB100:TestPoint_SMD_1.5mm, F.Cu at (114.5, 30.0)
- added TP057: TEST OUT9_SWITCHED, PB100:TestPoint_SMD_1.5mm, F.Cu at (117.2, 30.0)
- added TP058: TEST OUT10_CTL, PB100:TestPoint_SMD_1.5mm, F.Cu at (131.5, 3.20)
- added TP059: TEST OUT10_FLT, PB100:TestPoint_SMD_1.5mm, F.Cu at (134.2, 3.20)
- added TP060: TEST OUT10_IMON, PB100:TestPoint_SMD_1.5mm, F.Cu at (136.9, 3.20)
- added TP061: TEST OUT10_SWITCHED, PB100:TestPoint_SMD_1.5mm, F.Cu at (126.2, 6.70)
- added TP062: TEST Q1_GATE, PB100:TestPoint_SMD_1.5mm, B.Cu at (15.2, 25.6)
- added TP063: TEST Q2_GATE, PB100:TestPoint_SMD_1.5mm, B.Cu at (17.9, 25.6)
- added TP064: TEST INPUT_COMMON_SOURCE, PB100:TestPoint_SMD_1.5mm, B.Cu at (20.6, 25.6)
- added TP065: TEST VBAT_PROT_PRELINK, PB100:TestPoint_SMD_1.5mm, B.Cu at (23.4, 25.6)
- added U101: TPS48110AQDGXRQ1, PB100:VSSOP-20_19P-L5.0-W3.0-P0.50-LS5.0-BL_PE16, B.Cu at (46.3, 23.8)
- added U102: TPS48110AQDGXRQ1, PB100:VSSOP-20_19P-L5.0-W3.0-P0.50-LS5.0-BL_PE16, B.Cu at (79.5, 23.8)
- added U103: TPS48110AQDGXRQ1, PB100:VSSOP-20_19P-L5.0-W3.0-P0.50-LS5.0-BL_PE16, B.Cu at (19.0, 54.0)
- added U104: TPS48110AQDGXRQ1, PB100:VSSOP-20_19P-L5.0-W3.0-P0.50-LS5.0-BL_PE16, B.Cu at (35.5, 58.0)
- added U105: TPS48110AQDGXRQ1, PB100:VSSOP-20_19P-L5.0-W3.0-P0.50-LS5.0-BL_PE16, B.Cu at (51.0, 58.0)
- added U106: TPS48110AQDGXRQ1, PB100:VSSOP-20_19P-L5.0-W3.0-P0.50-LS5.0-BL_PE16, B.Cu at (67.0, 58.0)
- added U107: TPS48110AQDGXRQ1, PB100:VSSOP-20_19P-L5.0-W3.0-P0.50-LS5.0-BL_PE16, B.Cu at (83.0, 58.0)
- added U108: TPS48110AQDGXRQ1, PB100:VSSOP-20_19P-L5.0-W3.0-P0.50-LS5.0-BL_PE16, B.Cu at (99.0, 58.0)
- added U109: TPS48110AQDGXRQ1, PB100:VSSOP-20_19P-L5.0-W3.0-P0.50-LS5.0-BL_PE16, B.Cu at (115.0, 58.0)
- added U110: TPS48110AQDGXRQ1, PB100:VSSOP-20_19P-L5.0-W3.0-P0.50-LS5.0-BL_PE16, B.Cu at (131.0, 58.0)
- added U2: INA228AQDGSRQ1 TOTAL CURRENT MONITOR, PB100:VSSOP-10_L3.0-W3.0-P0.50-LS4.9-BL, B.Cu at (24.5, 43.0)
- added U3: LM5164QDDATQ1 100V 1A BUCK, PB100:SOIC-8_L4.9-W3.9-P1.27-LS6.0-BL-EP2.9, F.Cu at (124.0, 14.0)
- added W101: OUT1 PCB PIGTAIL TO OFF-BOARD FUSE/SEALED CONNECTOR, PB100:POWER_PIGTAIL_2xTH_20A, F.Cu at (50.0, 4.50)
- added W102: OUT2 PCB PIGTAIL TO OFF-BOARD FUSE/SEALED CONNECTOR, PB100:POWER_PIGTAIL_2xTH_20A, F.Cu at (100.0, 4.50)
- added W103: OUT3 PCB PIGTAIL TO OFF-BOARD FUSE/SEALED CONNECTOR, PB100:POWER_PIGTAIL_2xTH_20A, F.Cu at (19.0, 85.5)
- added W104: OUT4 PCB PIGTAIL TO OFF-BOARD FUSE/SEALED CONNECTOR, PB100:POWER_PIGTAIL_2xTH_20A, F.Cu at (35.0, 85.5)
- added W105: OUT5 PCB PIGTAIL TO OFF-BOARD FUSE/SEALED CONNECTOR, PB100:POWER_PIGTAIL_2xTH_20A, F.Cu at (51.0, 85.5)
- added W106: OUT6 PCB PIGTAIL TO OFF-BOARD FUSE/SEALED CONNECTOR, PB100:POWER_PIGTAIL_2xTH_20A, F.Cu at (67.0, 85.5)
- added W107: OUT7 PCB PIGTAIL TO OFF-BOARD FUSE/SEALED CONNECTOR, PB100:POWER_PIGTAIL_2xTH_20A, F.Cu at (83.0, 85.5)
- added W108: OUT8 PCB PIGTAIL TO OFF-BOARD FUSE/SEALED CONNECTOR, PB100:POWER_PIGTAIL_2xTH_20A, F.Cu at (99.0, 85.5)
- added W109: OUT9 PCB PIGTAIL TO OFF-BOARD FUSE/SEALED CONNECTOR, PB100:POWER_PIGTAIL_2xTH_20A, F.Cu at (115.0, 85.5)
- added W110: OUT10 PCB PIGTAIL TO OFF-BOARD FUSE/SEALED CONNECTOR, PB100:POWER_PIGTAIL_2xTH_20A, F.Cu at (131.0, 85.5)
- D1, U1: moved to B.Cu
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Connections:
- Q1 pad 1: Q1_DGATE -> Q1_GATE
- Q101 pad 2: OUT1_SRC -> OUT1_SWITCHED
- Q101 pad 3: OUT1_SRC -> OUT1_SWITCHED
- Q101 pad 4: OUT1_SRC -> OUT1_SWITCHED
- Q101 pad 5: OUT1_SRC -> OUT1_SWITCHED
- Q101 pad 6: OUT1_SRC -> OUT1_SWITCHED
- Q101 pad 7: OUT1_SRC -> OUT1_SWITCHED
- Q101 pad 8: OUT1_SRC -> OUT1_SWITCHED
- Q101 pad Tab: OUT1_SWITCHED -> OUT1_FET_DRAIN
- Q102 pad 2: OUT2_SRC -> OUT2_SWITCHED
- Q102 pad 3: OUT2_SRC -> OUT2_SWITCHED
- Q102 pad 4: OUT2_SRC -> OUT2_SWITCHED
- Q102 pad 5: OUT2_SRC -> OUT2_SWITCHED
- Q102 pad 6: OUT2_SRC -> OUT2_SWITCHED
- Q102 pad 7: OUT2_SRC -> OUT2_SWITCHED
- Q102 pad 8: OUT2_SRC -> OUT2_SWITCHED
- Q102 pad Tab: OUT2_SWITCHED -> OUT2_FET_DRAIN
- Q103 pad 2: OUT3_SRC -> OUT3_SWITCHED
- Q103 pad 3: OUT3_SRC -> OUT3_SWITCHED
- Q103 pad 4: OUT3_SRC -> OUT3_SWITCHED
- Q103 pad 5: OUT3_SRC -> OUT3_SWITCHED
- Q103 pad 6: OUT3_SRC -> OUT3_SWITCHED
- Q103 pad 7: OUT3_SRC -> OUT3_SWITCHED
- Q103 pad 8: OUT3_SRC -> OUT3_SWITCHED
- Q103 pad Tab: OUT3_SWITCHED -> OUT3_FET_DRAIN
- Q104 pad 2: OUT4_SRC -> OUT4_SWITCHED
- Q104 pad 3: OUT4_SRC -> OUT4_SWITCHED
- Q104 pad 4: OUT4_SRC -> OUT4_SWITCHED
- Q104 pad 5: OUT4_SRC -> OUT4_SWITCHED
- Q104 pad 6: OUT4_SRC -> OUT4_SWITCHED
- Q104 pad 7: OUT4_SRC -> OUT4_SWITCHED
- Q104 pad 8: OUT4_SRC -> OUT4_SWITCHED
- Q104 pad Tab: OUT4_SWITCHED -> OUT4_FET_DRAIN
- Q105 pad 2: OUT5_SRC -> OUT5_SWITCHED
- Q105 pad 3: OUT5_SRC -> OUT5_SWITCHED
- Q105 pad 4: OUT5_SRC -> OUT5_SWITCHED
- Q105 pad 5: OUT5_SRC -> OUT5_SWITCHED
- Q105 pad 6: OUT5_SRC -> OUT5_SWITCHED
- Q105 pad 7: OUT5_SRC -> OUT5_SWITCHED
- Q105 pad 8: OUT5_SRC -> OUT5_SWITCHED
- Q105 pad Tab: OUT5_SWITCHED -> OUT5_FET_DRAIN
- Q106 pad 2: OUT6_SRC -> OUT6_SWITCHED
- Q106 pad 3: OUT6_SRC -> OUT6_SWITCHED
- Q106 pad 4: OUT6_SRC -> OUT6_SWITCHED
- Q106 pad 5: OUT6_SRC -> OUT6_SWITCHED
- Q106 pad 6: OUT6_SRC -> OUT6_SWITCHED
- Q106 pad 7: OUT6_SRC -> OUT6_SWITCHED
- Q106 pad 8: OUT6_SRC -> OUT6_SWITCHED
- Q106 pad Tab: OUT6_SWITCHED -> OUT6_FET_DRAIN
- Q107 pad 2: OUT7_SRC -> OUT7_SWITCHED
- Q107 pad 3: OUT7_SRC -> OUT7_SWITCHED
- Q107 pad 4: OUT7_SRC -> OUT7_SWITCHED
- Q107 pad 5: OUT7_SRC -> OUT7_SWITCHED
- Q107 pad 6: OUT7_SRC -> OUT7_SWITCHED
- Q107 pad 7: OUT7_SRC -> OUT7_SWITCHED
- Q107 pad 8: OUT7_SRC -> OUT7_SWITCHED
- Q107 pad Tab: OUT7_SWITCHED -> OUT7_FET_DRAIN
- Q108 pad 2: OUT8_SRC -> OUT8_SWITCHED
- Q108 pad 3: OUT8_SRC -> OUT8_SWITCHED
- Q108 pad 4: OUT8_SRC -> OUT8_SWITCHED
- Q108 pad 5: OUT8_SRC -> OUT8_SWITCHED
- Q108 pad 6: OUT8_SRC -> OUT8_SWITCHED
- Q108 pad 7: OUT8_SRC -> OUT8_SWITCHED
- Q108 pad 8: OUT8_SRC -> OUT8_SWITCHED
- Q108 pad Tab: OUT8_SWITCHED -> OUT8_FET_DRAIN
- Q109 pad 2: OUT9_SRC -> OUT9_SWITCHED
- Q109 pad 3: OUT9_SRC -> OUT9_SWITCHED
- Q109 pad 4: OUT9_SRC -> OUT9_SWITCHED
- Q109 pad 5: OUT9_SRC -> OUT9_SWITCHED
- Q109 pad 6: OUT9_SRC -> OUT9_SWITCHED
- Q109 pad 7: OUT9_SRC -> OUT9_SWITCHED
- Q109 pad 8: OUT9_SRC -> OUT9_SWITCHED
- Q109 pad Tab: OUT9_SWITCHED -> OUT9_FET_DRAIN
- Q110 pad 2: OUT10_SRC -> OUT10_SWITCHED
- Q110 pad 3: OUT10_SRC -> OUT10_SWITCHED
- Q110 pad 4: OUT10_SRC -> OUT10_SWITCHED
- Q110 pad 5: OUT10_SRC -> OUT10_SWITCHED
- Q110 pad 6: OUT10_SRC -> OUT10_SWITCHED
- Q110 pad 7: OUT10_SRC -> OUT10_SWITCHED
- Q110 pad 8: OUT10_SRC -> OUT10_SWITCHED
- Q110 pad Tab: OUT10_SWITCHED -> OUT10_FET_DRAIN
- Q2 pad 1: Q2_HGATE -> Q2_GATE
- U1 pad 10: unconnected-(U1-IMON-Pad10) -> (no net)
- U1 pad 17: unconnected-(U1-N.C.-Pad17) -> (no net)
- U1 pad 21: unconnected-(U1-N.C.-Pad21) -> (no net)
- U1 pad 25: unconnected-(U1-RTN-Pad25) -> (no net)
- U1 pad 3: unconnected-(U1-SW-Pad3) -> (no net)
- U1 pad 8: unconnected-(U1-N.C.-Pad8) -> (no net)
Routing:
- net LB_3V3_IO: track 0.00 -> 359.1 mm, vias 0 -> 16
- net VBAT_PROT: track 0.00 -> 328.9 mm, vias 0 -> 126
- net PB_5V_OUT: track 0.00 -> 210.7 mm, vias 0 -> 6
- net PB_I2C_INT: track 0.00 -> 155.4 mm, vias 0 -> 5
- net VBAT_RAW: track 0.00 -> 152.6 mm, vias 0 -> 6
- net PB_I2C_SCL: track 0.00 -> 148.2 mm, vias 0 -> 5
- net OUT3_FLT: track 0.00 -> 138.8 mm, vias 0 -> 4
- net OUT4_FLT: track 0.00 -> 131.1 mm, vias 0 -> 6
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- added copper zone on B.Cu, net GND
- added copper zone on F.Cu, net GND
- added copper zone on In2.Cu, net GND
- added copper zone on F.Cu, net INPUT_COMMON_SOURCE
- added copper zone on F.Cu, net OUT10_FET_DRAIN
- added copper zone on B.Cu, net OUT10_SWITCHED
- added copper zone on F.Cu, net OUT10_SWITCHED
- added copper zone on F.Cu, net OUT1_FET_DRAIN
- added copper zone on F.Cu, net OUT1_SWITCHED
- added copper zone on F.Cu, net OUT2_FET_DRAIN
- added copper zone on F.Cu, net OUT2_SWITCHED
- added copper zone on F.Cu, net OUT3_FET_DRAIN
- added copper zone on B.Cu, net OUT3_SWITCHED
- added copper zone on F.Cu, net OUT3_SWITCHED
- added copper zone on F.Cu, net OUT4_FET_DRAIN
- added copper zone on B.Cu, net OUT4_SWITCHED
- added copper zone on F.Cu, net OUT4_SWITCHED
- added copper zone on F.Cu, net OUT5_FET_DRAIN
- added copper zone on B.Cu, net OUT5_SWITCHED
- added copper zone on F.Cu, net OUT5_SWITCHED
- added copper zone on F.Cu, net OUT6_FET_DRAIN
- added copper zone on B.Cu, net OUT6_SWITCHED
- added copper zone on F.Cu, net OUT6_SWITCHED
- added copper zone on F.Cu, net OUT7_FET_DRAIN
- added copper zone on B.Cu, net OUT7_SWITCHED
- added copper zone on F.Cu, net OUT7_SWITCHED
- added copper zone on F.Cu, net OUT8_FET_DRAIN
- added copper zone on B.Cu, net OUT8_SWITCHED
- added copper zone on F.Cu, net OUT8_SWITCHED
- added copper zone on F.Cu, net OUT9_FET_DRAIN
- added copper zone on B.Cu, net OUT9_SWITCHED
- added copper zone on F.Cu, net OUT9_SWITCHED
- added copper zone on In5.Cu, net VBAT_PROT
- added copper zone on B.Cu, net VBAT_PROT_PRELINK
- added copper zone on F.Cu, net VBAT_PROT_PRELINK
- added copper zone on F.Cu, net VBAT_RAW
- added copper zone on B.Cu, net VBAT_REV_PROT
- added copper zone on F.Cu, net VBAT_REV_PROT
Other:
- copper layers 4 -> 8
- board text added: "VALUE-BEARING EVT LAYOUT - FAB REVIEW REQUIRED"
- board text removed: "PARTIAL SCHEMATIC IMPORT - FAB REVIEW BLOCKED"

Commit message: Close PB-100 EVT connectivity
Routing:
- net OUT4_FET_DRAIN: track 1.49 -> 121.8 mm, vias 0 -> 2
- net OUT7_SWITCHED: track 2.87 -> 102.4 mm, vias 0 -> 7
- net OUT4_SWITCHED: track 15.7 -> 90.0 mm, vias 3 -> 7
- net OUT3_IWRN: track 0.00 -> 65.8 mm, vias 0 -> 2
- net OUT7_TMR: track 0.00 -> 65.2 mm, vias 0 -> 3
- net OUT4_TMR: track 0.00 -> 62.5 mm, vias 0 -> 4
- net OUT2_OV: track 1.50 -> 48.9 mm, vias 0 -> 7
- net GND: track 19.9 -> 60.0 mm, vias 105 -> 127
- net OUT2_FLT: track 35.8 -> 67.3 mm, vias 3 -> 6
- net OUT5_CTL: track 80.5 -> 102.6 mm, vias 6 -> 9
- net VBAT_REV_PROT: track 35.5 -> 55.8 mm, vias 16 -> 19
- net OUT8_CS_P: track 0.00 -> 19.6 mm, vias 0 -> 2
- net VBAT_PROT: track 328.9 -> 345.1 mm, vias 126 -> 131
- net OUT8_SWITCHED: track 73.7 -> 88.4 mm, vias 5 -> 7
- net OUT2_FET_DRAIN: track 19.3 -> 26.3 mm, vias 3 -> 5
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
